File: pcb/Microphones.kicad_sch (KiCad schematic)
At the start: 36 parts, among them U1 AD8426ACPZ-R7, U2 AD8426ACPZ-R7

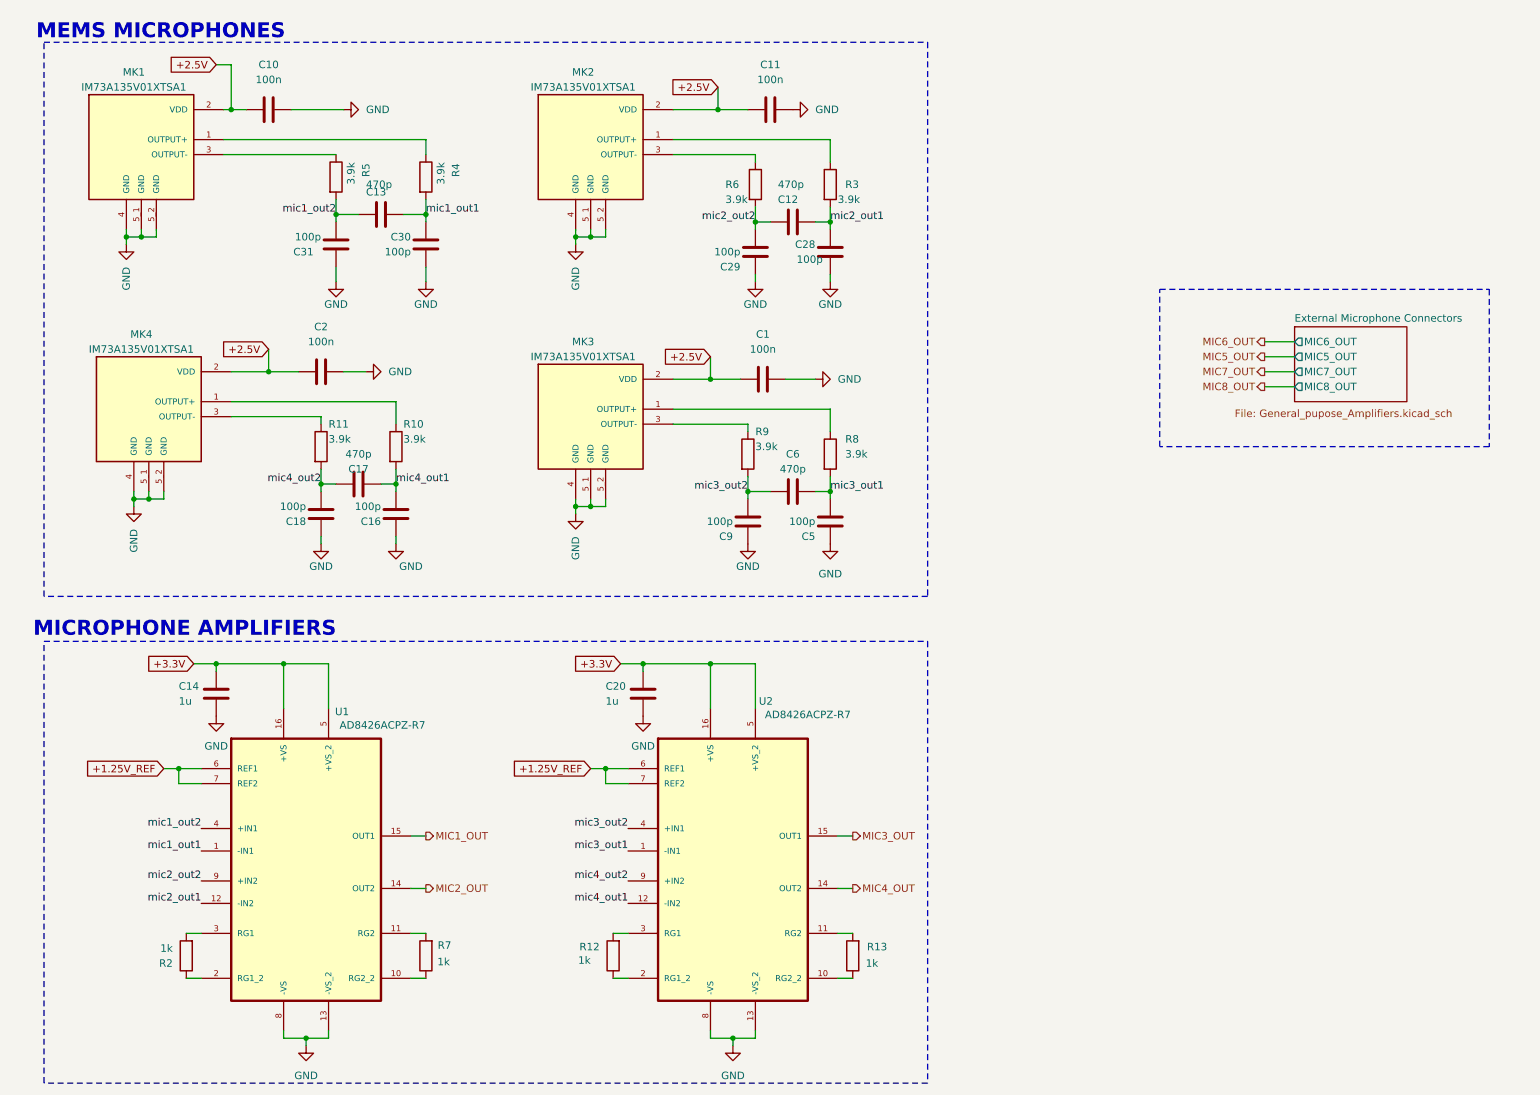
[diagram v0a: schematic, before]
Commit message: Progress in pcb routing
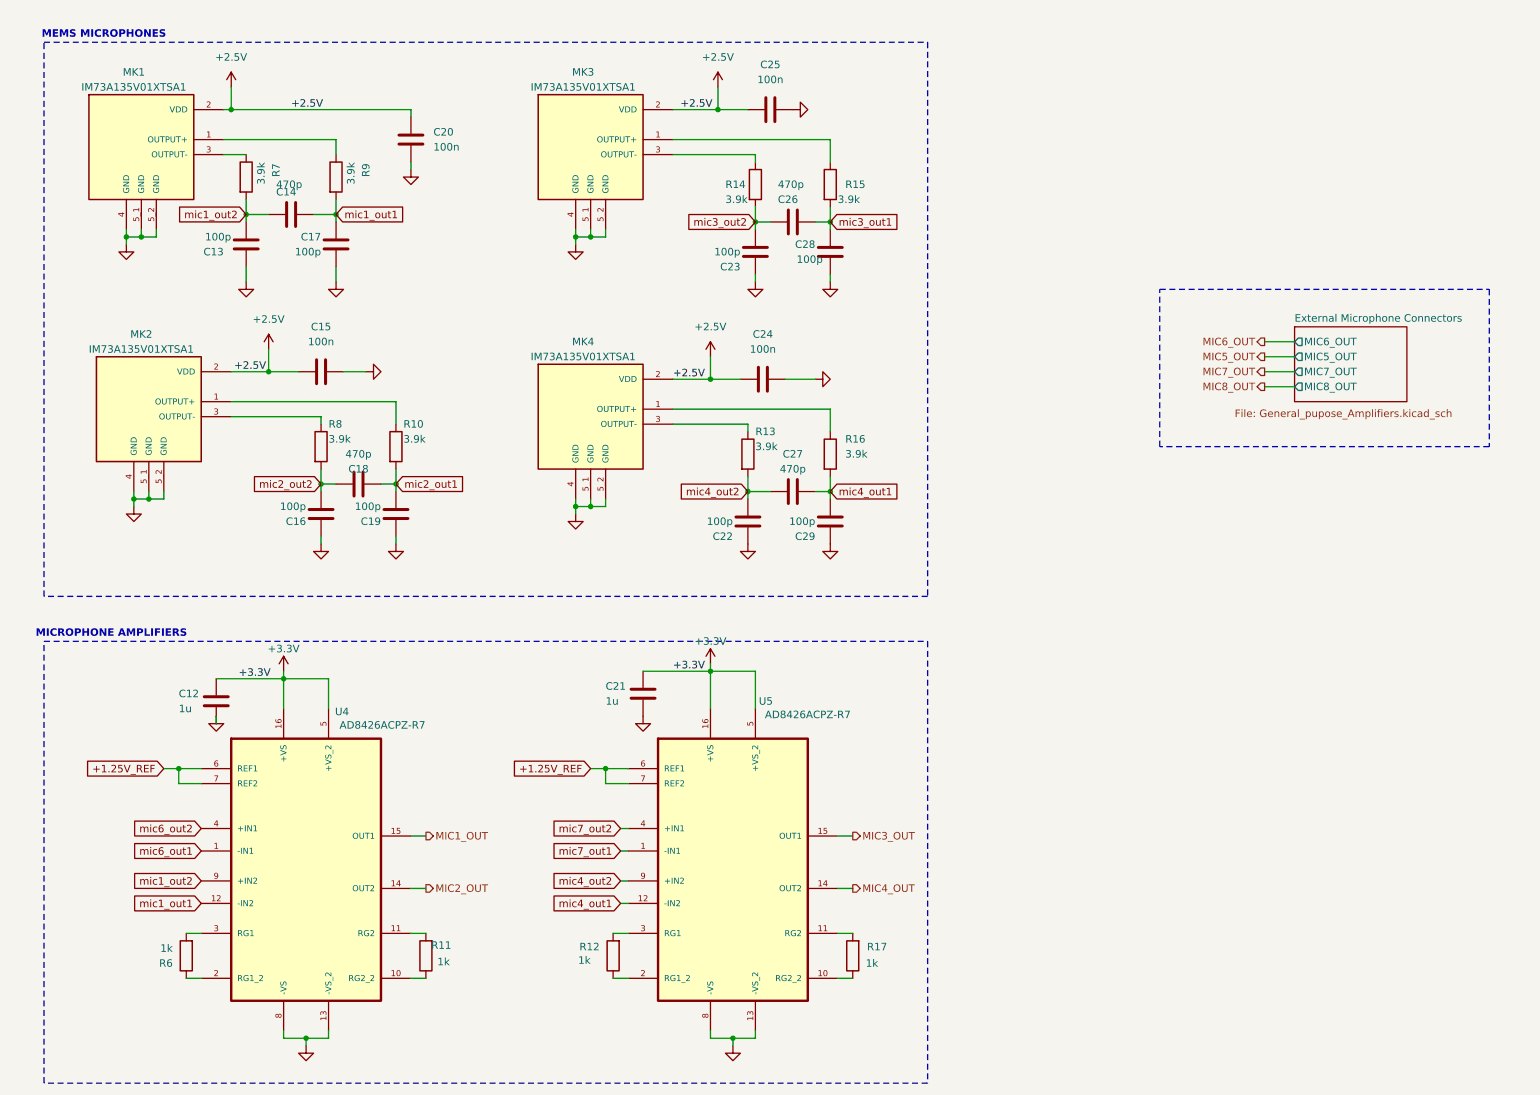
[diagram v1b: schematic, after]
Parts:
- renumbered C14 to C12, C31 to C13, C13 to C14, C2 to C15, C18 to C16, C30 to C17, C17 to C18, C16 to C19, C10 to C20, C20 to C21, C9 to C22, C29 to C23, C1 to C24, C11 to C25, C12 to C26, C6 to C27, C5 to C29, MK4 to MK2, MK2 to MK3, MK3 to MK4, R7 to R11, R9 to R13, R6 to R14, R3 to R15, R8 to R16, R13 to R17, R2 to R6, R5 to R7, R11 to R8, R4 to R9, U1 to U4, U2 to U5
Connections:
- net mic1_out1: now also U4.12 (-IN2); no longer U4.1 (-IN1)
- net mic1_out2: now also U4.9 (+IN2); no longer U4.4 (+IN1)
- net mic2_out1: now also C18.1, C19.2, R10.2; no longer C26.1, C28.2, R15.2, U4.12 (-IN2)
- net mic2_out2: now also C16.2, C18.2, R8.2; no longer C23.2, C26.2, R14.2, U4.9 (+IN2)
- net mic3_out1: now also C26.1, C28.2, R15.2; no longer C27.1, C29.2, R16.2, U5.1 (-IN1)
- net mic3_out2: now also C23.2, C26.2, R14.2; no longer C22.2, C27.2, R13.2, U5.4 (+IN1)
- net mic4_out1: now also C27.1, C29.2, R16.2; no longer C18.1, C19.2, R10.2
- net mic4_out2: now also C22.2, C27.2, R13.2; no longer C16.2, C18.2, R8.2
- new net mic6_out1: U4.1 (-IN1)
- new net mic6_out2: U4.4 (+IN1)
- new net mic7_out1: U5.1 (-IN1)
- new net mic7_out2: U5.4 (+IN1)
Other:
- moved on the sheet: C12, C13, C14, C17, C20, R7, R9

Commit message: pcb layout polishing
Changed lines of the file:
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@@
 	(wire
 		(pts
-			(xy 124.46 124.46) (xy 135.89 124.46)
-		)
-		(stroke
-			(width 0)
-			(type default)
-		)
-	)
-	(wire
-		(pts
 			(xy 143.51 45.72) (xy 143.51 48.26)
 		)
@@
 	(wire
 		(pts
+			(xy 124.46 124.46) (xy 135.89 124.46)
+		)
+		(stroke
+			(width 0)
+			(type default)
+		)
+	)
+	(wire
+		(pts
 			(xy 140.97 74.93) (xy 135.89 74.93)
 		)
@@
 		)
 	)
-	(label "+3.3V"
-		(at 55.88 125.73 0)
-		(effects
-			(font
-				(size 1.27 1.27)
-			)
-			(justify left bottom)
-		)
-	)
 	(label "+2.5V"
 		(at 129.54 74.93 0)
@@
 		)
 	)
-	(label "+3.3V"
-		(at 129.54 124.46 0)
-		(effects
-			(font
-				(size 1.27 1.27)
-			)
-			(justify left bottom)
-		)
-	)
 	(label "+2.5V"
 		(at 64.77 29.21 0)
@@
 		)
 		(property "Value" "+3.3V"
-			(at 63.5 120.65 0)
+			(at 67.31 123.19 0)
 			(effects
 				(font
@@
 		)
 		(property "Value" "+3.3V"
-			(at 135.89 119.38 0)
+			(at 139.7 121.92 0)
 			(effects
 				(font

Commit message: in works
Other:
- title: SensEdu 0.7 -> SensEdu 0.9
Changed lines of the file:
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@@
 	(paper "A4")
 	(title_block
-		(title "SensEdu 0.7")
+		(title "SensEdu 0.9")
 		(date "2025-12-05")
 		(company "Infineon Technologies")

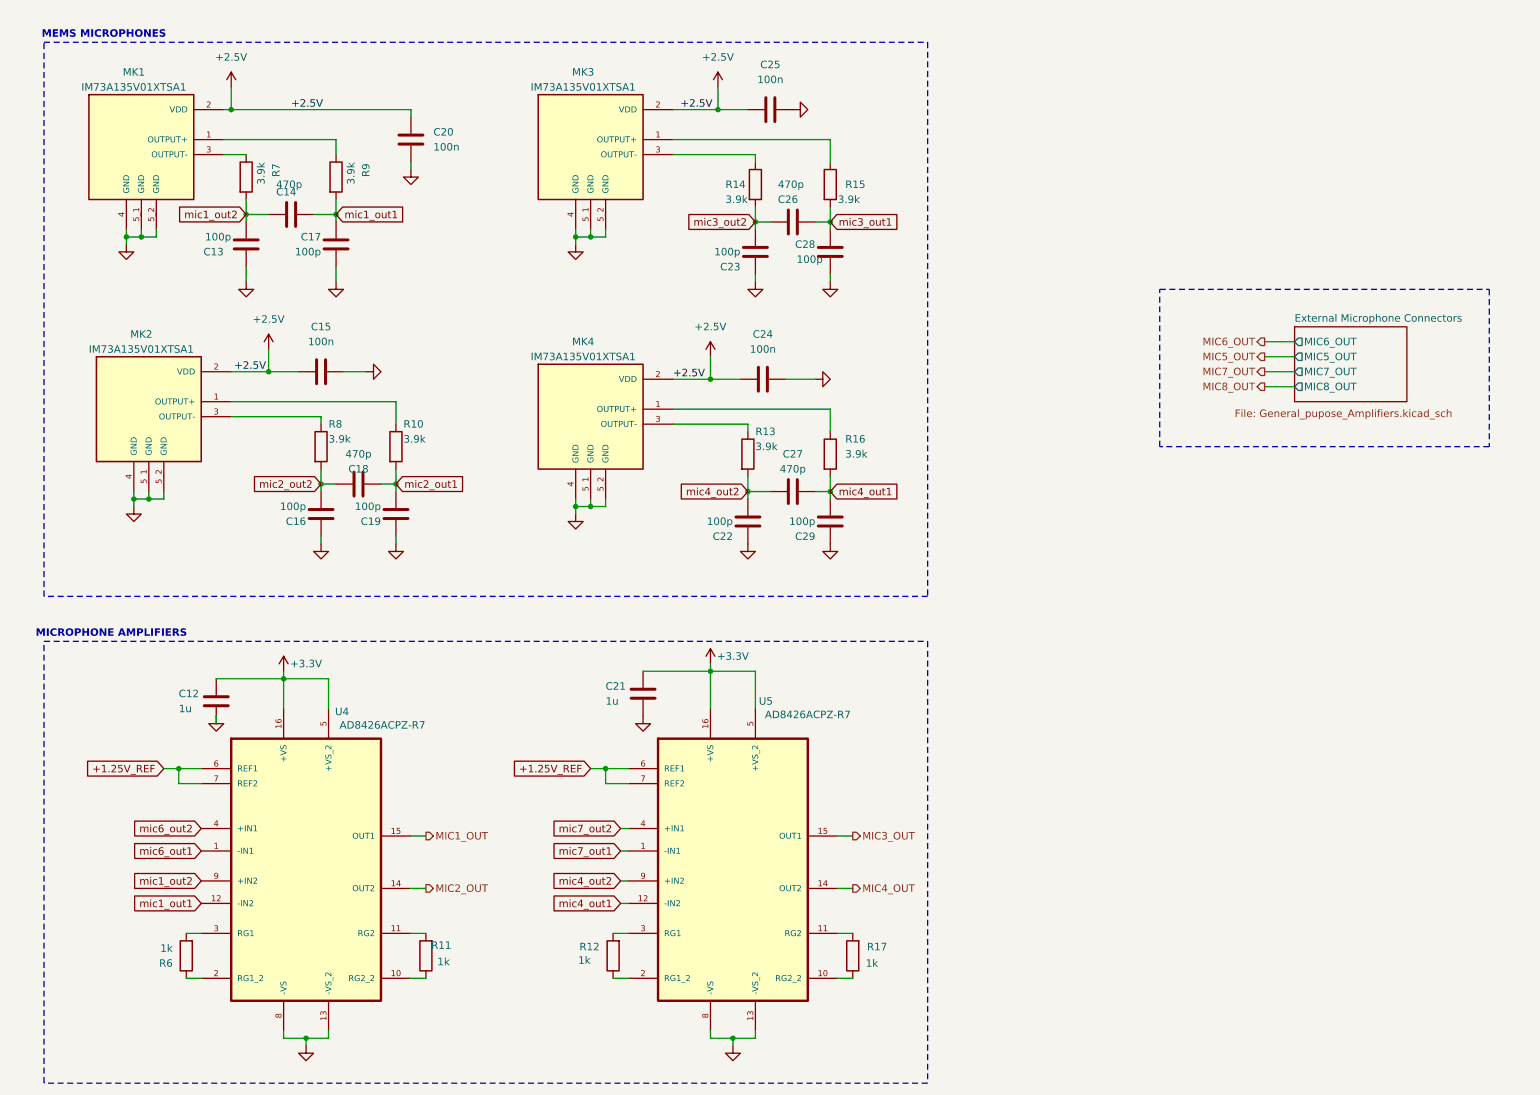
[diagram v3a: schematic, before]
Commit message: feat: Redraw PCB layout
- Change supply polarity and pin numbers of ADA4511
- Change cap of switches to 100n to reduce bom
- Change supply of sensors to unison 3.3V
- Rearrange mic and amps pins
- Add mountains
- Add Infineon logo
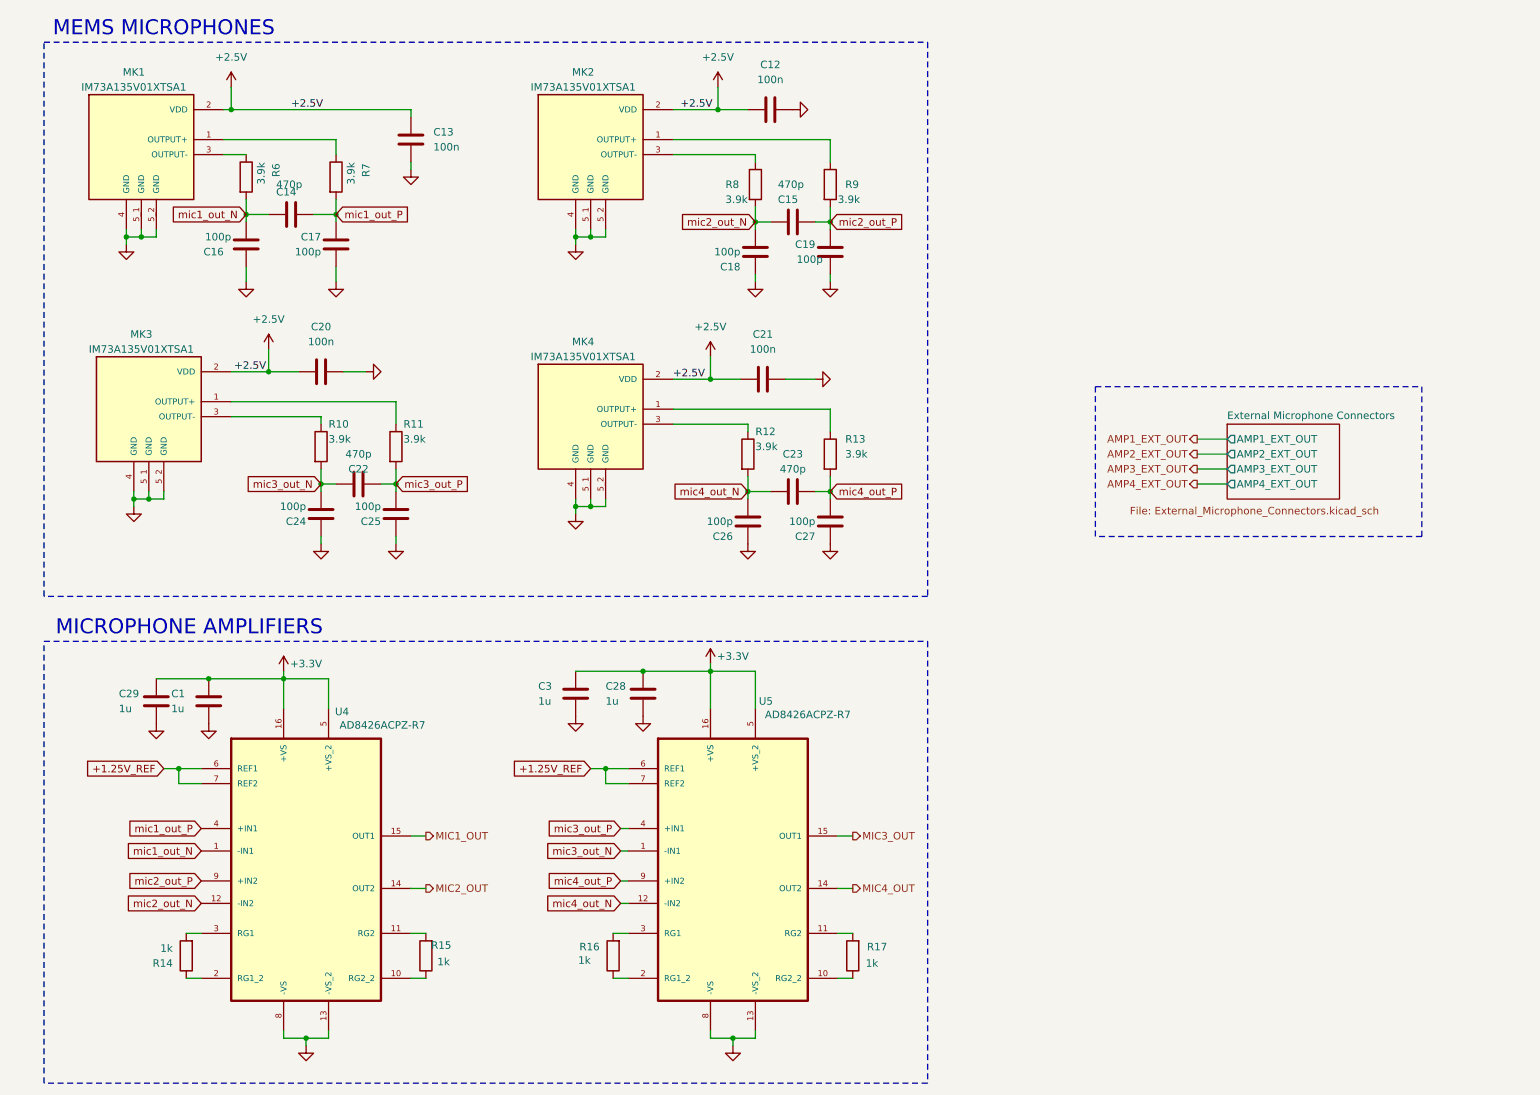
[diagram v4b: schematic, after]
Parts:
- added C1, C3: 1u, Capacitor_SMD:C_0603_1608Metric, symbol SensEdu:C
- C12: renamed from C25; footprint Capacitor_SMD:C_0805_2012Metric -> Capacitor_SMD:C_0603_1608Metric; symbol Device:C -> SensEdu:C
- C13: renamed from C20; footprint Capacitor_SMD:C_0805_2012Metric -> Capacitor_SMD:C_0603_1608Metric; symbol Device:C -> SensEdu:C
- C14, C17: footprint Capacitor_SMD:C_0805_2012Metric -> Capacitor_SMD:C_0603_1608Metric; symbol Device:C -> SensEdu:C
- C15: renamed from C26; footprint Capacitor_SMD:C_0805_2012Metric -> Capacitor_SMD:C_0603_1608Metric; symbol Device:C -> SensEdu:C
- C16: renamed from C13; footprint Capacitor_SMD:C_0805_2012Metric -> Capacitor_SMD:C_0603_1608Metric; symbol Device:C -> SensEdu:C
- C18: renamed from C23; footprint Capacitor_SMD:C_0805_2012Metric -> Capacitor_SMD:C_0603_1608Metric; symbol Device:C -> SensEdu:C
- C19: renamed from C28; footprint Capacitor_SMD:C_0805_2012Metric -> Capacitor_SMD:C_0603_1608Metric; symbol Device:C -> SensEdu:C
- C20: renamed from C15; footprint Capacitor_SMD:C_0805_2012Metric -> Capacitor_SMD:C_0603_1608Metric; symbol Device:C -> SensEdu:C
- C21: renamed from C24; footprint Capacitor_SMD:C_0805_2012Metric -> Capacitor_SMD:C_0603_1608Metric; symbol Device:C -> SensEdu:C
- C22: renamed from C18; footprint Capacitor_SMD:C_0805_2012Metric -> Capacitor_SMD:C_0603_1608Metric; symbol Device:C -> SensEdu:C
- C23: renamed from C27; footprint Capacitor_SMD:C_0805_2012Metric -> Capacitor_SMD:C_0603_1608Metric; symbol Device:C -> SensEdu:C
- C24: renamed from C16; footprint Capacitor_SMD:C_0805_2012Metric -> Capacitor_SMD:C_0603_1608Metric; symbol Device:C -> SensEdu:C
- C25: renamed from C19; footprint Capacitor_SMD:C_0805_2012Metric -> Capacitor_SMD:C_0603_1608Metric; symbol Device:C -> SensEdu:C
- C26: renamed from C22; footprint Capacitor_SMD:C_0805_2012Metric -> Capacitor_SMD:C_0603_1608Metric; symbol Device:C -> SensEdu:C
- C27: renamed from C29; footprint Capacitor_SMD:C_0805_2012Metric -> Capacitor_SMD:C_0603_1608Metric; symbol Device:C -> SensEdu:C
- C28: renamed from C21; footprint Capacitor_SMD:C_0805_2012Metric -> Capacitor_SMD:C_0603_1608Metric; symbol Device:C -> SensEdu:C
- C29: renamed from C12; footprint Capacitor_SMD:C_0805_2012Metric -> Capacitor_SMD:C_0603_1608Metric; symbol Device:C -> SensEdu:C
- MK1, MK4: footprint MIC_IM73A135V01XTSA1 -> SensEdu:MIC_IM73A135V01XTSA1
- MK2: renamed from MK3; footprint MIC_IM73A135V01XTSA1 -> SensEdu:MIC_IM73A135V01XTSA1
- MK3: renamed from MK2; footprint MIC_IM73A135V01XTSA1 -> SensEdu:MIC_IM73A135V01XTSA1
- R10: renamed from R8; footprint Resistor_SMD:R_0805_2012Metric -> Resistor_SMD:R_0603_1608Metric; symbol Device:R -> SensEdu:R
- R11: renamed from R10; footprint Resistor_SMD:R_0805_2012Metric -> Resistor_SMD:R_0603_1608Metric; symbol Device:R -> SensEdu:R
- R12: renamed from R13; footprint Resistor_SMD:R_0805_2012Metric -> Resistor_SMD:R_0603_1608Metric; symbol Device:R -> SensEdu:R
- R13: renamed from R16; footprint Resistor_SMD:R_0805_2012Metric -> Resistor_SMD:R_0603_1608Metric; symbol Device:R -> SensEdu:R
- R14: renamed from R6; footprint Resistor_SMD:R_0805_2012Metric -> Resistor_SMD:R_0603_1608Metric; symbol Device:R -> SensEdu:R
- R15: renamed from R11; footprint Resistor_SMD:R_0805_2012Metric -> Resistor_SMD:R_0603_1608Metric; symbol Device:R -> SensEdu:R
- R16: renamed from R12; footprint Resistor_SMD:R_0805_2012Metric -> Resistor_SMD:R_0603_1608Metric; symbol Device:R -> SensEdu:R
- R17: footprint Resistor_SMD:R_0805_2012Metric -> Resistor_SMD:R_0603_1608Metric; symbol Device:R -> SensEdu:R
- R6: renamed from R7; footprint Resistor_SMD:R_0805_2012Metric -> Resistor_SMD:R_0603_1608Metric; symbol Device:R -> SensEdu:R
- R7: renamed from R9; footprint Resistor_SMD:R_0805_2012Metric -> Resistor_SMD:R_0603_1608Metric; symbol Device:R -> SensEdu:R
- R8: renamed from R14; footprint Resistor_SMD:R_0805_2012Metric -> Resistor_SMD:R_0603_1608Metric; symbol Device:R -> SensEdu:R
- R9: renamed from R15; footprint Resistor_SMD:R_0805_2012Metric -> Resistor_SMD:R_0603_1608Metric; symbol Device:R -> SensEdu:R
- U5: symbol SensEdu:AD8426ACPZ-R7 -> SensEdu:AD8426ACPZ-R7_1
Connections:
- net mic6_out1 is gone; now on net mic1_out_N: U4.1 (-IN1)
- net mic6_out2 is gone; now on net mic1_out_P: U4.4 (+IN1)
- net mic7_out1 is gone; now on net mic3_out_N: U5.1 (-IN1)
- net mic7_out2 is gone; now on net mic3_out_P: U5.4 (+IN1)
- net +3.3V: now also C1.1, C3.1
- net GND: now also C1.2, C3.2
- net mic1_out1 renamed mic1_out_P
- net mic1_out_P: no longer U4.12 (-IN2)
- net mic1_out2 renamed mic1_out_N
- net mic1_out_N: no longer U4.9 (+IN2)
- net mic2_out1 renamed mic3_out_P
- net mic2_out2 renamed mic3_out_N
- net mic3_out1 renamed mic2_out_P
- net mic2_out_P: now also U4.9 (+IN2)
- net mic3_out2 renamed mic2_out_N
- net mic2_out_N: now also U4.12 (-IN2)
- net mic4_out1 renamed mic4_out_P
- net mic4_out_P: now also U5.9 (+IN2); no longer U5.12 (-IN2)
- net mic4_out2 renamed mic4_out_N
- net mic4_out_N: now also U5.12 (-IN2); no longer U5.9 (+IN2)
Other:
- sheet External Microphone Connectors: file General_pupose_Amplifiers.kicad_sch -> External_Microphone_Connectors.kicad_sch
- sheet External Microphone Connectors ports: added AMP1_EXT_OUT, AMP2_EXT_OUT, AMP3_EXT_OUT, AMP4_EXT_OUT; removed MIC5_OUT, MIC6_OUT, MIC7_OUT, MIC8_OUT
- moved on the sheet: C29

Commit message: refactor: Update PDF and information
- Add BOM
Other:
- title: SensEdu 0.9 -> SensEdu
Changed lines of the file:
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@@
 	(paper "A4")
 	(title_block
-		(title "SensEdu 0.9")
-		(date "2025-12-05")
+		(title "SensEdu")
+		(date "2026-02-26")
 		(rev "0.9")
 		(company "Infineon Technologies")
